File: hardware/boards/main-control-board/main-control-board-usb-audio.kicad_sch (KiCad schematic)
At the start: 1 part

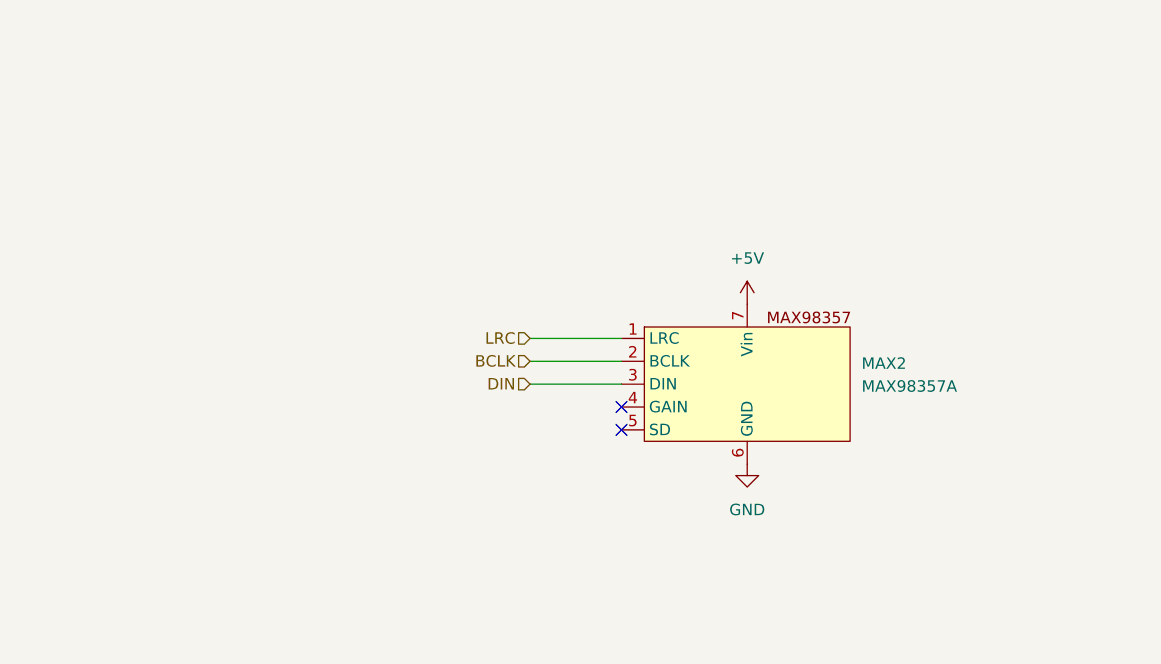
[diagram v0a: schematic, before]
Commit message: integrate audio module
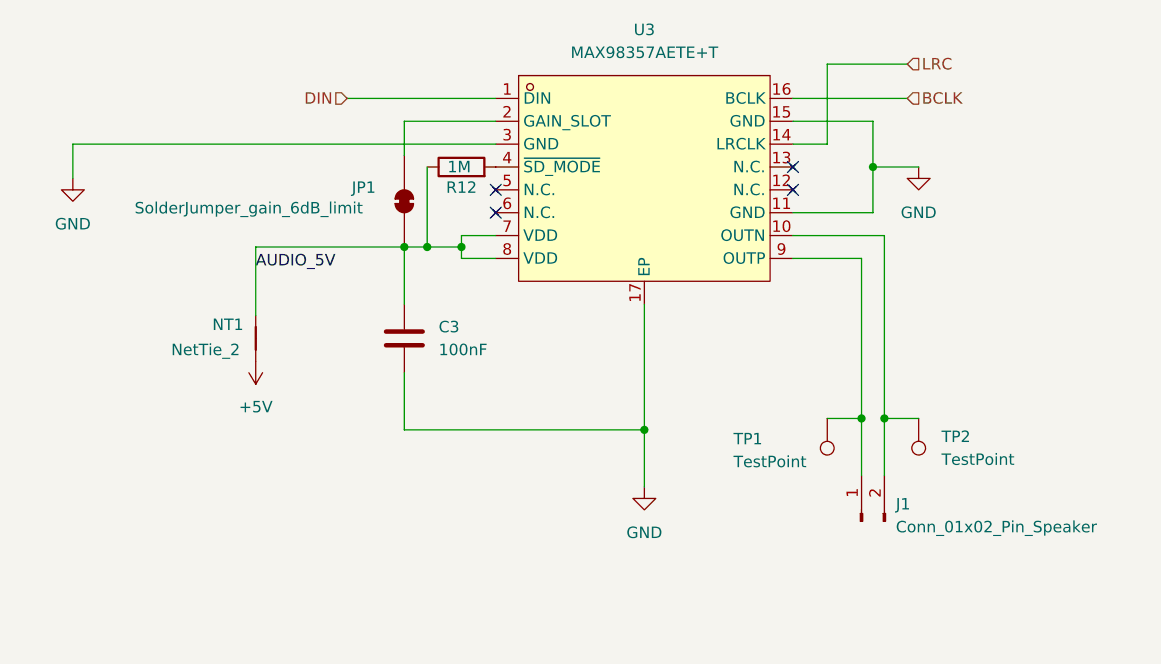
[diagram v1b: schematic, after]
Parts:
- removed MAX2: MAX98357A, symbol TinyEngineerModules:MAX98357_Module
- added C3: 100nF, Capacitor_SMD:C_0603_1608Metric, symbol Device:C
- added J1: Conn_01x02_Pin_Speaker, Connector_Molex:Molex_PicoBlade_53261-0271_1x02-1MP_P1.25mm_Horizontal, symbol Connector:Conn_01x02_Pin
- added JP1: SolderJumper_gain_6dB_limit, Jumper:SolderJumper-2_P1.3mm_Bridged_RoundedPad1.0x1.5mm, symbol Jumper:SolderJumper_2_Bridged
- added NT1: NetTie_2, NetTie:NetTie-2_SMD_Pad2.0mm, symbol Device:NetTie_2
- added R12: 1M, Resistor_SMD:R_0603_1608Metric, symbol Device:R
- added TP1, TP2: TestPoint, Connector_Wire:SolderWire-0.25sqmm_1x01_D0.65mm_OD2mm, symbol Connector:TestPoint
- added U3: MAX98357AETE+T, easyeda:TQFN-16_L3.0-W3.0-P0.50-BL-EP1.5, symbol easyeda:MAX98357AETE+T
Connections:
- net +5V: now also NT1.1
- net BCLK: now also U3.16 (BCLK)
- net DIN: now also U3.1 (DIN)
- net GND: now also C3.1, U3.11 (GND), U3.15 (GND), U3.17 (EP), U3.3 (GND)
- net LRC: now also U3.14 (LRCLK)
- new net: JP1.2 (B), U3.2 (GAIN_SLOT)
- new net: R12.2, U3.4 (~{SD_MODE})
- new net: J1.2 (Pin_2), TP2.1, U3.10 (OUTN)
- new net: J1.1 (Pin_1), TP1.1, U3.9 (OUTP)
- new net AUDIO_5V: C3.2, JP1.1 (A), NT1.2, R12.1, U3.7 (VDD), U3.8 (VDD)
- no-connect marks 2 -> 4

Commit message: improve board visuals
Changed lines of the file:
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@@
 		(at 158.75 62.23)
 	)
-	(wire
-		(pts
-			(xy 99.06 68.58) (xy 99.06 76.2)
+	(junction
+		(at 99.06 74.93)
+		(diameter 0)
+		(color 0 0 0 0)
+	)
+	(wire
+		(pts
+			(xy 99.06 68.58) (xy 99.06 74.93)
+		)
+		(stroke
+			(width 0)
+			(type default)
+		)
+	)
+	(wire
+		(pts
+			(xy 99.06 74.93) (xy 99.06 76.2)
 		)
 		(stroke
@@
 		)
 	)
+	(symbol
+		(lib_id "power:PWR_FLAG")
+		(at 99.06 74.93 0)
+		(unit 1)
+		(body_style 1)
+		(exclude_from_sim no)
+		(in_bom yes)
+		(on_board yes)
+		(in_pos_files yes)
+		(dnp no)
+		(property "Reference" "#FLG03"
+			(at 99.06 73.025 0)
+			(hide yes)
+			(show_name no)
+			(do_not_autoplace no)
+			(effects
+				(font
+					(size 1.27 1.27)
+				)
+			)
+		)
+		(property "Value" "PWR_FLAG"
+			(at 99.06 69.85 0)
+			(show_name no)
+			(do_not_autoplace no)
+			(effects
+				(font
+					(size 1.27 1.27)
+				)
+			)
+		)
+		(property "Footprint" ""
+			(at 99.06 74.93 0)
+			(hide yes)
+			(show_name no)
+			(do_not_autoplace no)
+			(effects
+				(font
+					(size 1.27 1.27)
+				)
+			)
+		)
+		(property "Datasheet" ""
+			(at 99.06 74.93 0)
+			(hide yes)
+			(show_name no)
+			(do_not_autoplace no)
+			(effects
+				(font
+					(size 1.27 1.27)
+				)
+			)
+		)
+		(property "Description" "Special symbol for telling ERC where power comes from"
+			(at 99.06 74.93 0)
+			(hide yes)
+			(show_name no)
+			(do_not_autoplace no)
+			(effects
+				(font
+					(size 1.27 1.27)
+				)
+			)
+		)
+		(pin "1"
+		)
+		(instances
+			(project "main-control-board"
+				(path "/82a78d11-58ff-455c-a94e-f7463ce9fc2e/fe9c0ff4-ff93-486d-af4d-0d3b12e4783b"
+					(reference "#FLG03")
+					(unit 1)
+				)
+			)
+		)
+	)

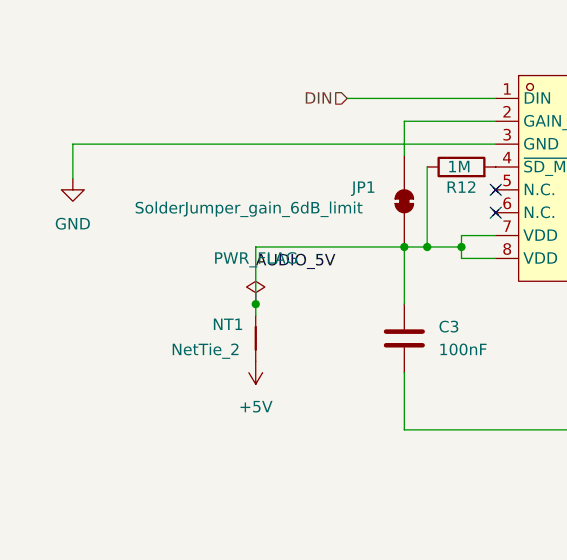
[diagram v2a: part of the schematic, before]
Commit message: add I2C extension port
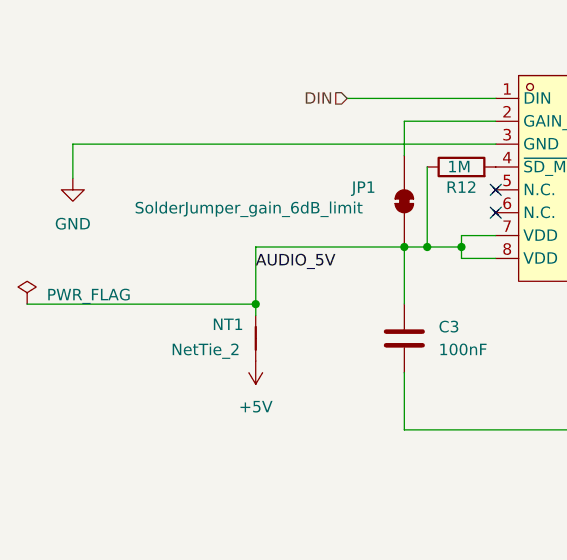
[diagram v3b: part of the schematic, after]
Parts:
- TP1, TP2: now left out of the parts list

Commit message: use basic components over extended
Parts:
- C3: LCSC Part # C1590 -> C14663
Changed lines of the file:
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@@
 			)
 		)
-		(property "LCSC Part #" "C1590"
+		(property "LCSC Part #" "C14663"
 			(at 115.57 78.74 90)
 			(hide yes)

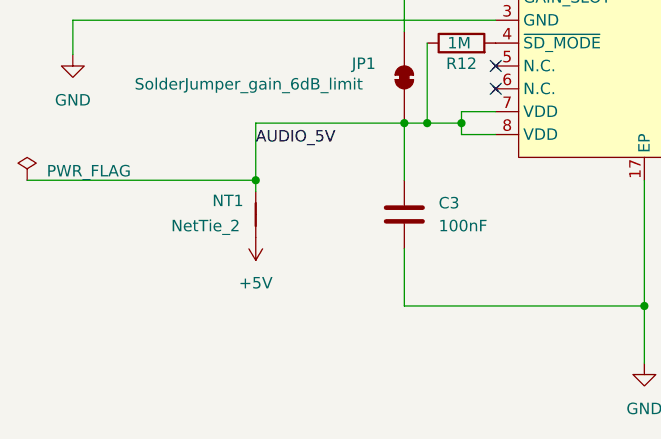
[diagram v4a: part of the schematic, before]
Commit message: add polyfuse protection
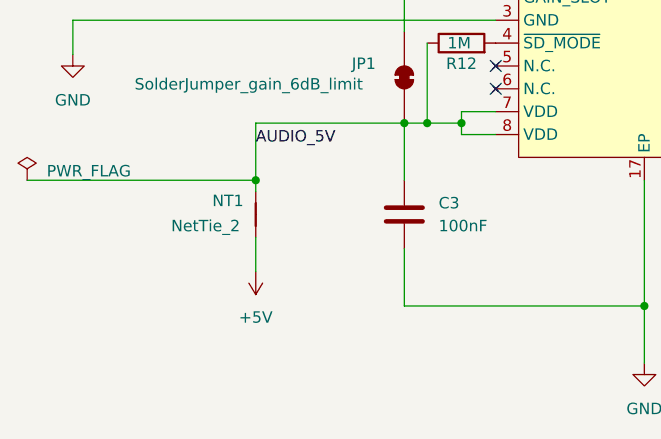
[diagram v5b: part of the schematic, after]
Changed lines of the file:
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@@
+	(wire
+		(pts
+			(xy 99.06 85.09) (xy 99.06 81.28)
+		)
+		(stroke
+			(width 0)
+			(type default)
+		)
+	)
 	(wire
 		(pts
@@
 	(symbol
 		(lib_id "power:+5V")
-		(at 99.06 81.28 180)
+		(at 99.06 85.09 180)
 		(unit 1)
 		(body_style 1)
@@
 		(fields_autoplaced yes)
 		(property "Reference" "#PWR013"
-			(at 99.06 77.47 0)
+			(at 99.06 81.28 0)
 			(hide yes)
 			(show_name no)
@@
 		)
 		(property "Value" "+5V"
-			(at 99.06 86.36 0)
+			(at 99.06 90.17 0)
 			(show_name no)
 			(do_not_autoplace no)
@@
 		)
 		(property "Footprint" ""
-			(at 99.06 81.28 0)
+			(at 99.06 85.09 0)
 			(hide yes)
 			(show_name no)
@@
 		)
 		(property "Datasheet" ""
-			(at 99.06 81.28 0)
+			(at 99.06 85.09 0)
 			(hide yes)
 			(show_name no)
@@
 		)
 		(property "Description" "Power symbol creates a global label with name \"+5V\""
-			(at 99.06 81.28 0)
-			(hide yes)
-			(show_name no)
+			(at 99.06 85.09 0)
+			(hide yes)
+			(show_name no)

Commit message: pre-fab improvements
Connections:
- net at J1.2 (Pin_2), TP2.1: now also U3.9 (OUTP); no longer U3.10 (OUTN)
- net at J1.1 (Pin_1), TP1.1: now also U3.10 (OUTN); no longer U3.9 (OUTP)
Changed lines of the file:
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@@
 	(paper "A4")
 	(junction
+		(at 115.57 68.58)
+		(diameter 0)
+		(color 0 0 0 0)
+	)
+	(junction
+		(at 166.37 87.63)
+		(diameter 0)
+		(color 0 0 0 0)
+	)
+	(junction
+		(at 99.06 74.93)
+		(diameter 0)
+		(color 0 0 0 0)
+	)
+	(junction
+		(at 167.64 59.69)
+		(diameter 0)
+		(color 0 0 0 0)
+	)
+	(junction
+		(at 142.24 88.9)
+		(diameter 0)
+		(color 0 0 0 0)
+	)
+	(junction
 		(at 168.91 87.63)
-		(diameter 0)
-		(color 0 0 0 0)
-	)
-	(junction
-		(at 115.57 68.58)
-		(diameter 0)
-		(color 0 0 0 0)
-	)
-	(junction
-		(at 166.37 87.63)
-		(diameter 0)
-		(color 0 0 0 0)
-	)
-	(junction
-		(at 99.06 74.93)
-		(diameter 0)
-		(color 0 0 0 0)
-	)
-	(junction
-		(at 167.64 59.69)
-		(diameter 0)
-		(color 0 0 0 0)
-	)
-	(junction
-		(at 142.24 88.9)
 		(diameter 0)
 		(color 0 0 0 0)
@@
 	(wire
 		(pts
-			(xy 166.37 69.85) (xy 166.37 87.63)
+			(xy 166.37 67.31) (xy 166.37 87.63)
 		)
 		(stroke
@@
 	(wire
 		(pts
-			(xy 168.91 67.31) (xy 168.91 87.63)
-		)
-		(stroke
-			(width 0)
-			(type default)
-		)
-	)
-	(wire
-		(pts
 			(xy 162.56 57.15) (xy 158.75 57.15)
 		)
@@
 	(wire
 		(pts
-			(xy 158.75 69.85) (xy 166.37 69.85)
+			(xy 158.75 69.85) (xy 168.91 69.85)
 		)
 		(stroke
@@
 	(wire
 		(pts
-			(xy 158.75 67.31) (xy 168.91 67.31)
+			(xy 158.75 67.31) (xy 166.37 67.31)
 		)
 		(stroke
@@
 		)
 		(stroke
+			(width 0)
+			(type default)
+		)
+	)
+	(wire
+		(pts
+			(xy 168.91 69.85) (xy 168.91 87.63)
+		)
+		(stroke

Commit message: add efuse before 5V servo rail
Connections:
- net +5V renamed SERVO_5V
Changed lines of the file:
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@@
 	(wire
 		(pts
-			(xy 99.06 85.09) (xy 99.06 81.28)
+			(xy 99.06 81.28) (xy 99.06 100.33)
 		)
 		(stroke
@@
 			)
 			(justify left)
+		)
+	)
+	(hierarchical_label "SERVO_5V"
+		(shape passive)
+		(at 99.06 100.33 270)
+		(effects
+			(font
+				(size 1.27 1.27)
+			)
+			(justify right)
 		)
 	)
@@
 					(unit 1)
 				)
-			)
-		)
-	)
-	(symbol
-		(lib_id "power:+5V")
-		(at 99.06 85.09 180)
-		(unit 1)
-		(body_style 1)
-		(exclude_from_sim no)
-		(in_bom yes)
-		(on_board yes)
-		(in_pos_files yes)
-		(dnp no)
-		(fields_autoplaced yes)
-		(property "Reference" "#PWR013"
-			(at 99.06 81.28 0)
-			(hide yes)
-			(show_name no)
-			(do_not_autoplace no)
-			(effects
-				(font
-					(size 1.27 1.27)
-				)
-			)
-		)
-		(property "Value" "+5V"
-			(at 99.06 90.17 0)
-			(show_name no)
-			(do_not_autoplace no)
-			(effects
-				(font
-					(size 1.27 1.27)
-				)
-			)
-		)
-		(property "Footprint" ""
-			(at 99.06 85.09 0)
-			(hide yes)
-			(show_name no)
-			(do_not_autoplace no)
-			(effects
-				(font
-					(size 1.27 1.27)
-				)
-			)
-		)
-		(property "Datasheet" ""
-			(at 99.06 85.09 0)
-			(hide yes)
-			(show_name no)
-			(do_not_autoplace no)
-			(effects
-				(font
-					(size 1.27 1.27)
-				)
-			)
-		)
-		(property "Description" "Power symbol creates a global label with name \"+5V\""
-			(at 99.06 85.09 0)
-			(hide yes)
-			(show_name no)
-			(do_not_autoplace no)
-			(effects
-				(font
-					(size 1.27 1.27)
-				)
-			)
-		)
-		(pin "1"
-		)
-		(instances
-			(project "main-control-board"
-				(path "/82a78d11-58ff-455c-a94e-f7463ce9fc2e/fe9c0ff4-ff93-486d-af4d-0d3b12e4783b"
-					(reference "#PWR013")
-					(unit 1)
-				)

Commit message: feat(pcb): update component properties and add missing attributes
- Renamed connection values for ESP32 components to standardize naming.
- Added properties for KiLib_Generator, MPN, and Manufacturer for various components across multiple schematic files.
- Enhanced documentation for component attributes to improve clarity and accessibility in the design process.
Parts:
- C3: MPN (none) -> CC0603KRX7R9BB104; Manufacturer (none) -> YAGEO
- J1: MPN (none) -> HC-1.25-2PWT; Manufacturer (none) -> HCTL
- R12: MPN (none) -> 0603WAF1004T5E; Manufacturer (none) -> UNI-ROYAL(Uniroyal Elec)
- U3: LCSC Part C910544 -> (none); Manufacturer ADI(亚德诺)/MAXIM(美信) -> Analog Devices Inc./Maxim Integrated
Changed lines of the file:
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@@
+			)
+		)
+		(property "KiLib_Generator" ""
+			(at 115.57 63.5 90)
+			(hide yes)
+			(show_name no)
+			(do_not_autoplace no)
+			(effects
+				(font
+					(size 1.27 1.27)
+				)
 			)
 		)
@@
 		)
 		(property "LCSC Part #" "C22935"
+			(at 121.92 59.69 90)
+			(hide yes)
+			(show_name no)
+			(do_not_autoplace no)
+			(effects
+				(font
+					(size 1.27 1.27)
+				)
+			)
+		)
+		(property "KiLib_Generator" ""
+			(at 121.92 59.69 90)
+			(hide yes)
+			(show_name no)
+			(do_not_autoplace no)
+			(effects
+				(font
+					(size 1.27 1.27)
+				)
+			)
+		)
+		(property "MPN" "0603WAF1004T5E"
+			(at 121.92 59.69 90)
+			(hide yes)
+			(show_name no)
+			(do_not_autoplace no)
+			(effects
+				(font
+					(size 1.27 1.27)
+				)
+			)
+		)
+		(property "Manufacturer" "UNI-ROYAL(Uniroyal Elec)"
 			(at 121.92 59.69 90)
 			(hide yes)
@@
 			)
 		)
+		(property "KiLib_Generator" ""
+			(at 99.06 78.74 90)
+			(hide yes)
+			(show_name no)
+			(do_not_autoplace no)
+			(effects
+				(font
+					(size 1.27 1.27)
+				)
+			)
+		)
 		(pin "2"
 		)
@@
 			)
 		)
+		(property "KiLib_Generator" ""
+			(at 172.72 87.63 0)
+			(hide yes)
+			(show_name no)
+			(do_not_autoplace no)
+			(effects
+				(font
+					(size 1.27 1.27)
+				)
+			)
+		)
 		(pin "1"
 		)
@@
 		)
 		(property "Description" "test point"
+			(at 162.56 87.63 0)
+			(hide yes)
+			(show_name no)
+			(do_not_autoplace no)
+			(effects
+				(font
+					(size 1.27 1.27)
+				)
+			)
+		)
+		(property "KiLib_Generator" ""
 			(at 162.56 87.63 0)
 			(hide yes)
@@
 			)
 		)
+		(property "KiLib_Generator" ""
+			(at 166.37 99.06 90)
+			(hide yes)
+			(show_name no)
+			(do_not_autoplace no)
+			(effects
+				(font
+					(size 1.27 1.27)
+				)
+			)
+		)
+		(property "MPN" "HC-1.25-2PWT"
+			(at 166.37 99.06 90)
+			(hide yes)
+			(show_name no)
+			(do_not_autoplace no)
+			(effects
+				(font
+					(size 1.27 1.27)
+				)
+			)
+		)
+		(property "Manufacturer" "HCTL"
+			(at 166.37 99.06 90)
+			(hide yes)
+			(show_name no)
+			(do_not_autoplace no)
+			(effects
+				(font
+					(size 1.27 1.27)
+				)
+			)
+		)
 		(pin "2"
 		)
@@
 			)
 		)
+		(property "KiLib_Generator" ""
+			(at 115.57 78.74 0)
+			(hide yes)
+			(show_name no)
+			(do_not_autoplace no)
+			(effects
+				(font
+					(size 1.27 1.27)
+				)
+			)
+		)
+		(property "MPN" "CC0603KRX7R9BB104"
+			(at 115.57 78.74 0)
+			(hide yes)
+			(show_name no)
+			(do_not_autoplace no)
+			(effects
+				(font
+					(size 1.27 1.27)
+				)
+			)
+		)
+		(property "Manufacturer" "YAGEO"
+			(at 115.57 78.74 0)
+			(hide yes)
+			(show_name no)
+			(do_not_autoplace no)
+			(effects
+				(font
+					(size 1.27 1.27)
+				)
+			)
+		)
 		(pin "2"
 		)
@@
 			)
 		)
-		(property "Manufacturer" "ADI(亚德诺)/MAXIM(美信)"
+		(property "Manufacturer" "Analog Devices Inc./Maxim Integrated"
 			(at 142.24 87.63 0)
 			(hide yes)
@@
 			)
 		)
-		(property "LCSC Part" "C910544"
+		(property "LCSC Part" ""
 			(at 142.24 92.71 0)
 			(hide yes)
 			(show_name no)
+			(do_not_autoplace no)
+			(effects
+				(font
+					(size 1.27 1.27)
+				)
+			)
+		)
+		(property "KiLib_Generator" ""
+			(at 142.24 62.23 0)
+			(hide yes)
+			(show_name no)
